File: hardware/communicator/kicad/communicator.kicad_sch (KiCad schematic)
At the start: 0 parts

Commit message: feat: add R1 detailed hardware and navigation protocol review candidate
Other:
- added sheet 00_vehicle_input (00_vehicle_input.kicad_sch)
- added sheet 00b_reverse_ov (00b_reverse_ov.kicad_sch)
- added sheet 00c_auto_5v (00c_auto_5v.kicad_sch)
- added sheet 01_usb_c (01_usb_c.kicad_sch)
- added sheet 01b_usb_limit (01b_usb_limit.kicad_sch)
- added sheet 02_system_power (02_system_power.kicad_sch)
- added sheet 03_reset (03_reset.kicad_sch)
- added sheet 03b_phy_power (03b_phy_power.kicad_sch)
- added sheet 03c_auto_qualification (03c_auto_qualification.kicad_sch)
- added sheet 12b_latch_clear (12b_latch_clear.kicad_sch)
- added sheet 14_can_connectors (14_can_connectors.kicad_sch)
- added sheet 15_gnss_ins (15_gnss_ins.kicad_sch)
- added sheet 16_barometer (16_barometer.kicad_sch)
- added sheet 17_gps_ports (17_gps_ports.kicad_sch)
- added sheet 18_gps_protection (18_gps_protection.kicad_sch)
- added sheet 19_gps_power (19_gps_power.kicad_sch)
- added sheet 20_test_points (20_test_points.kicad_sch)

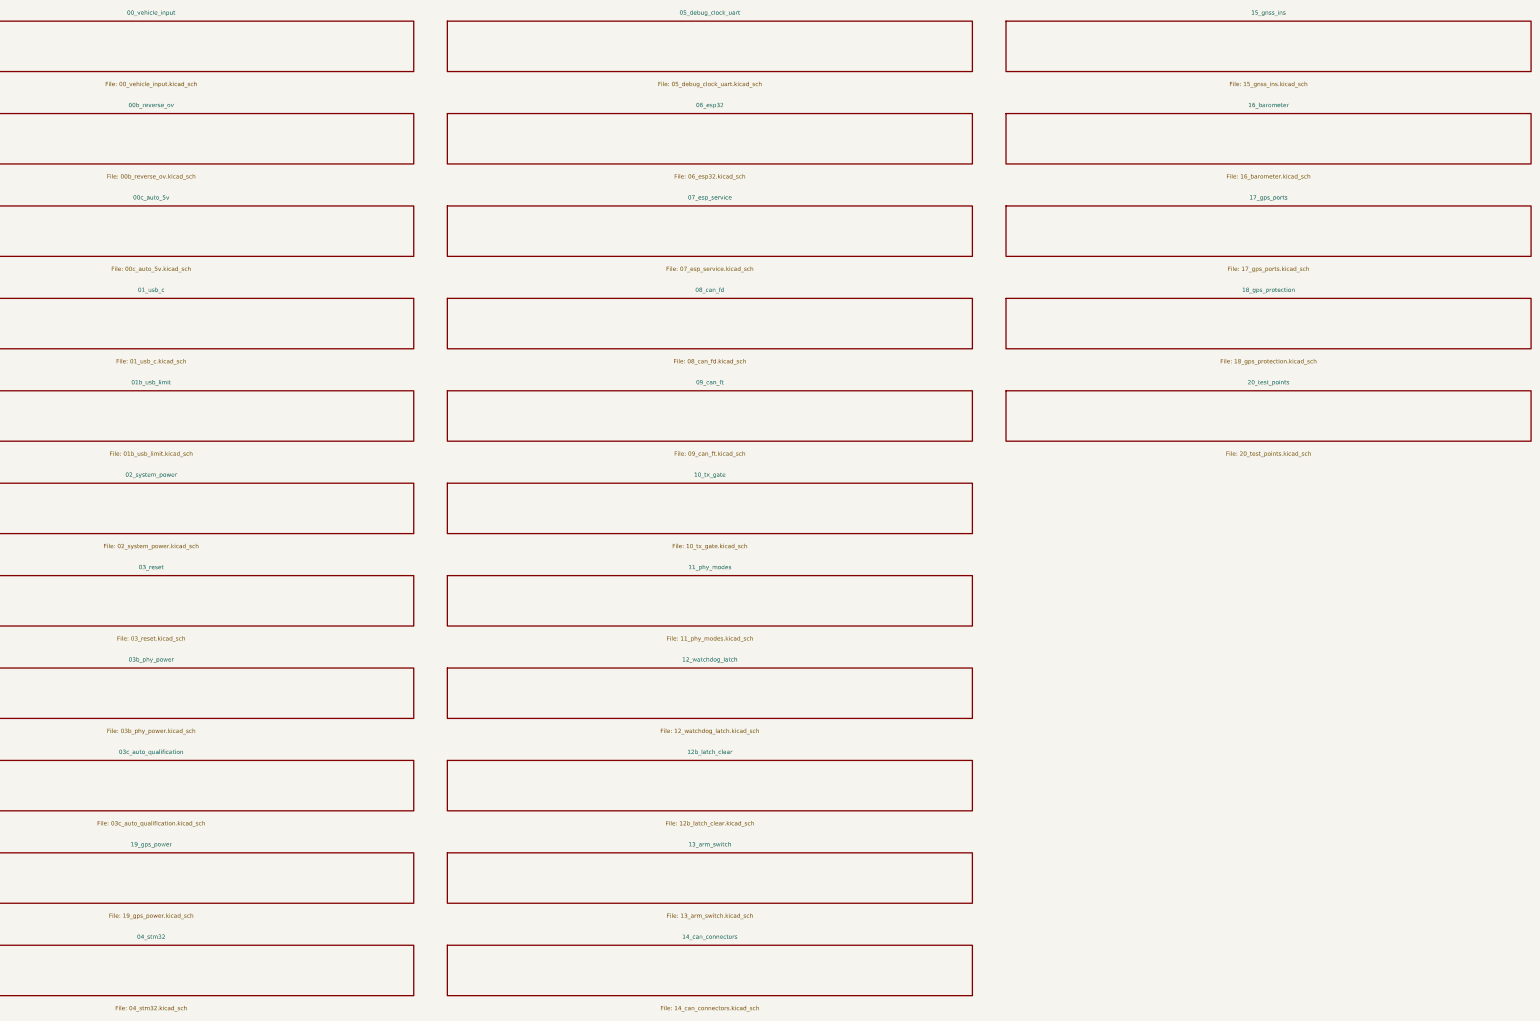
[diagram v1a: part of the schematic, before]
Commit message: fix: close hardware rail-fault paths and sensor contract gaps
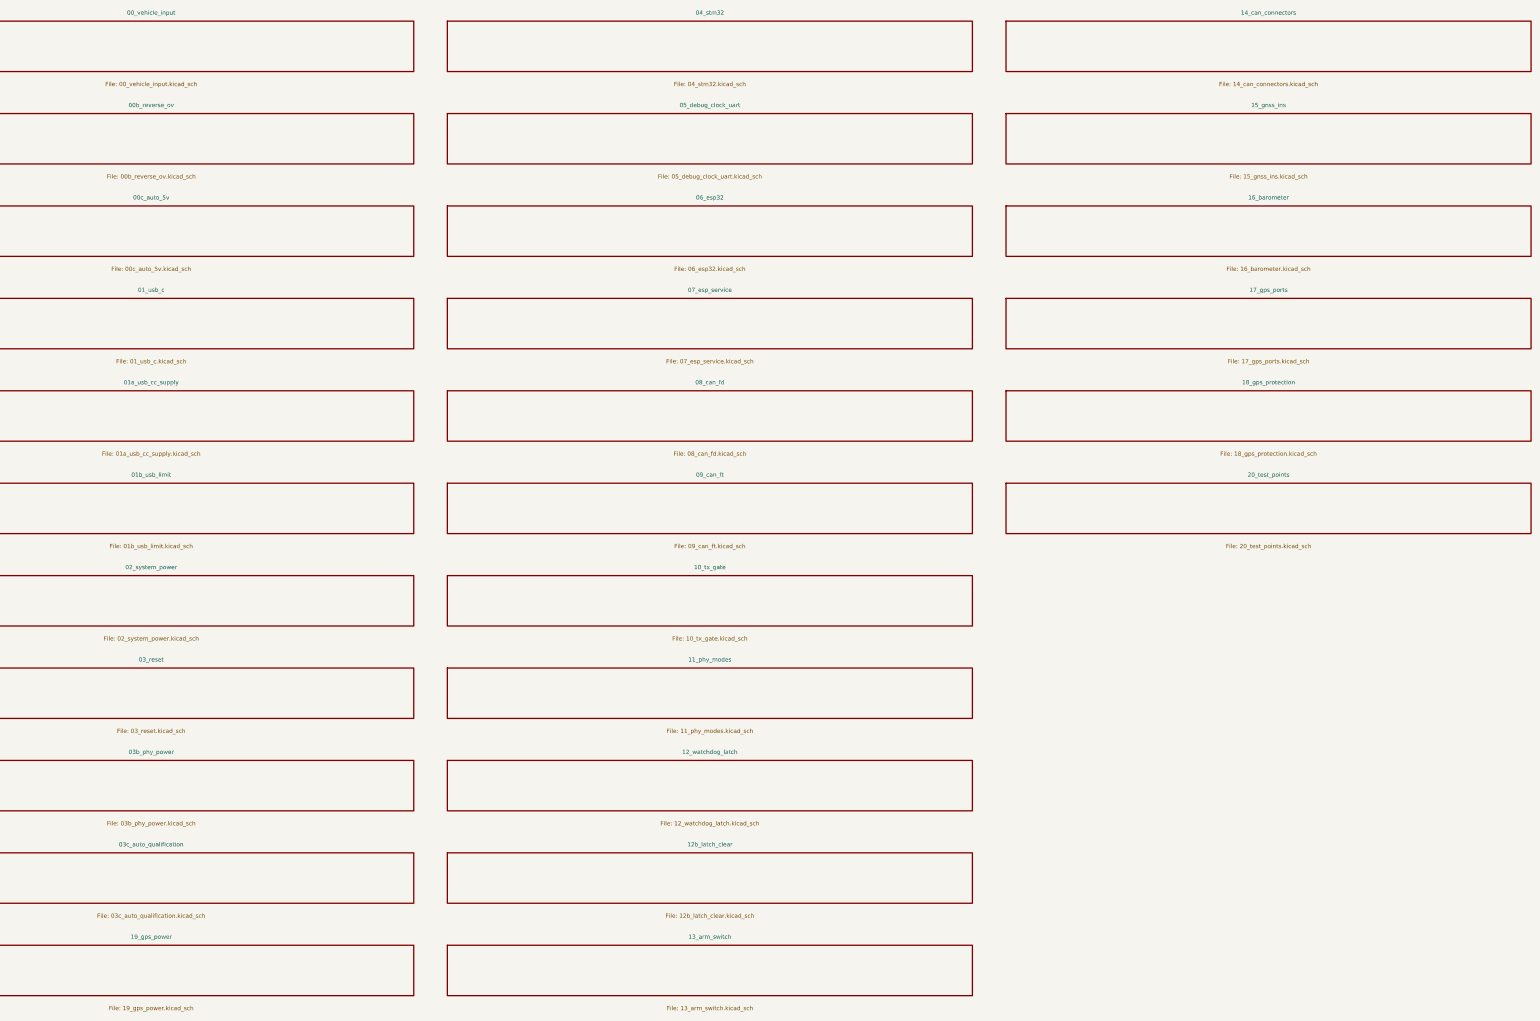
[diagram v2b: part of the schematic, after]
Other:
- added sheet 01a_usb_cc_supply (01a_usb_cc_supply.kicad_sch)

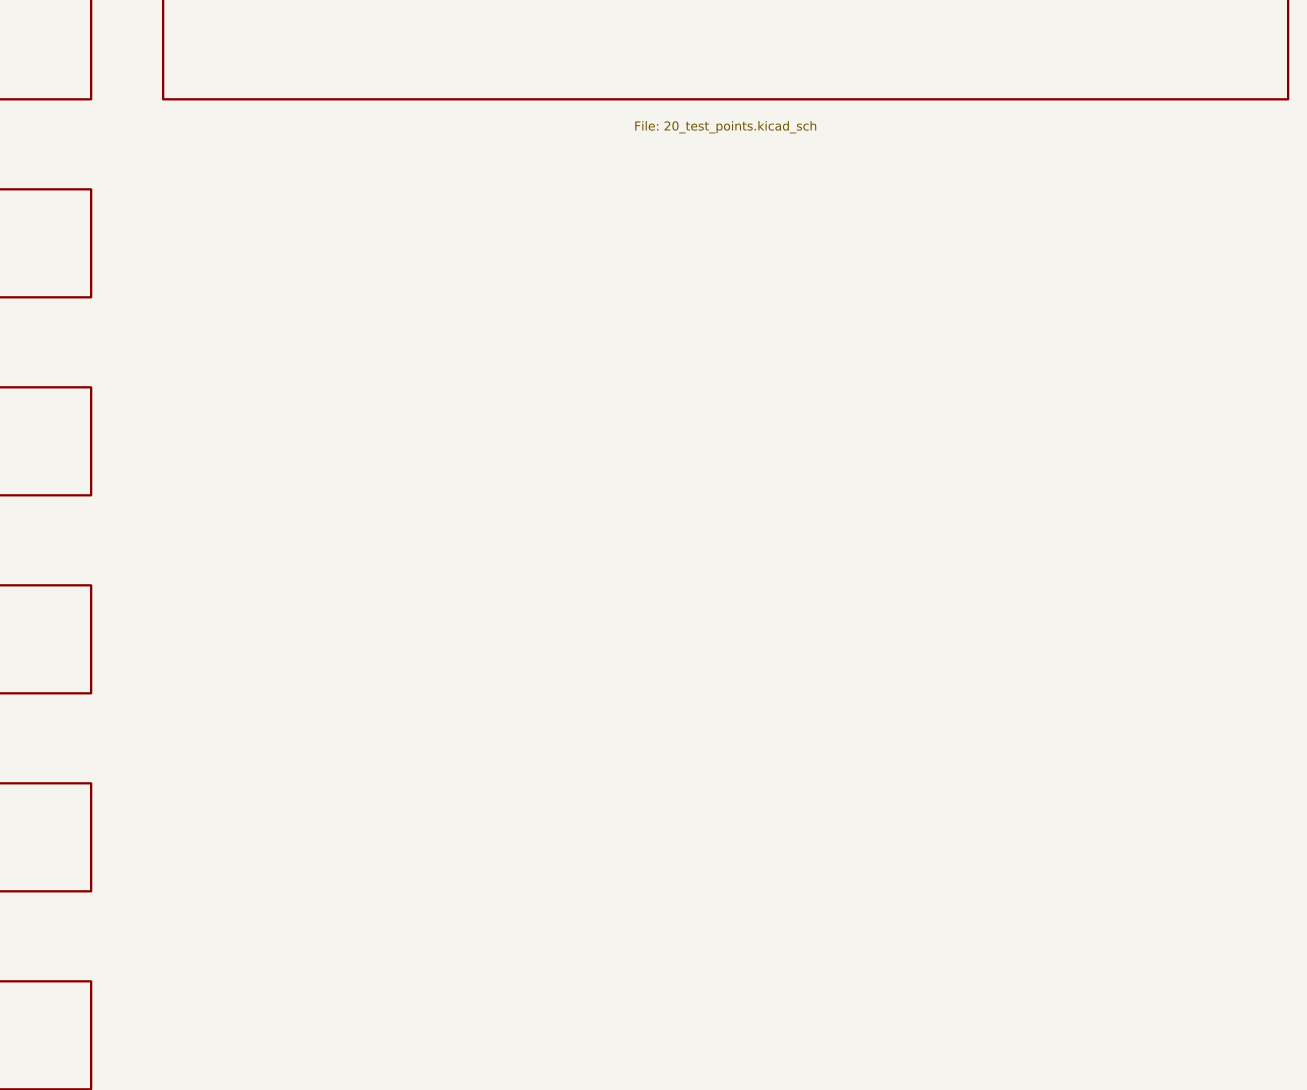
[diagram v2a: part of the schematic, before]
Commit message: Design independent OTA recovery and update N16R8 hardware
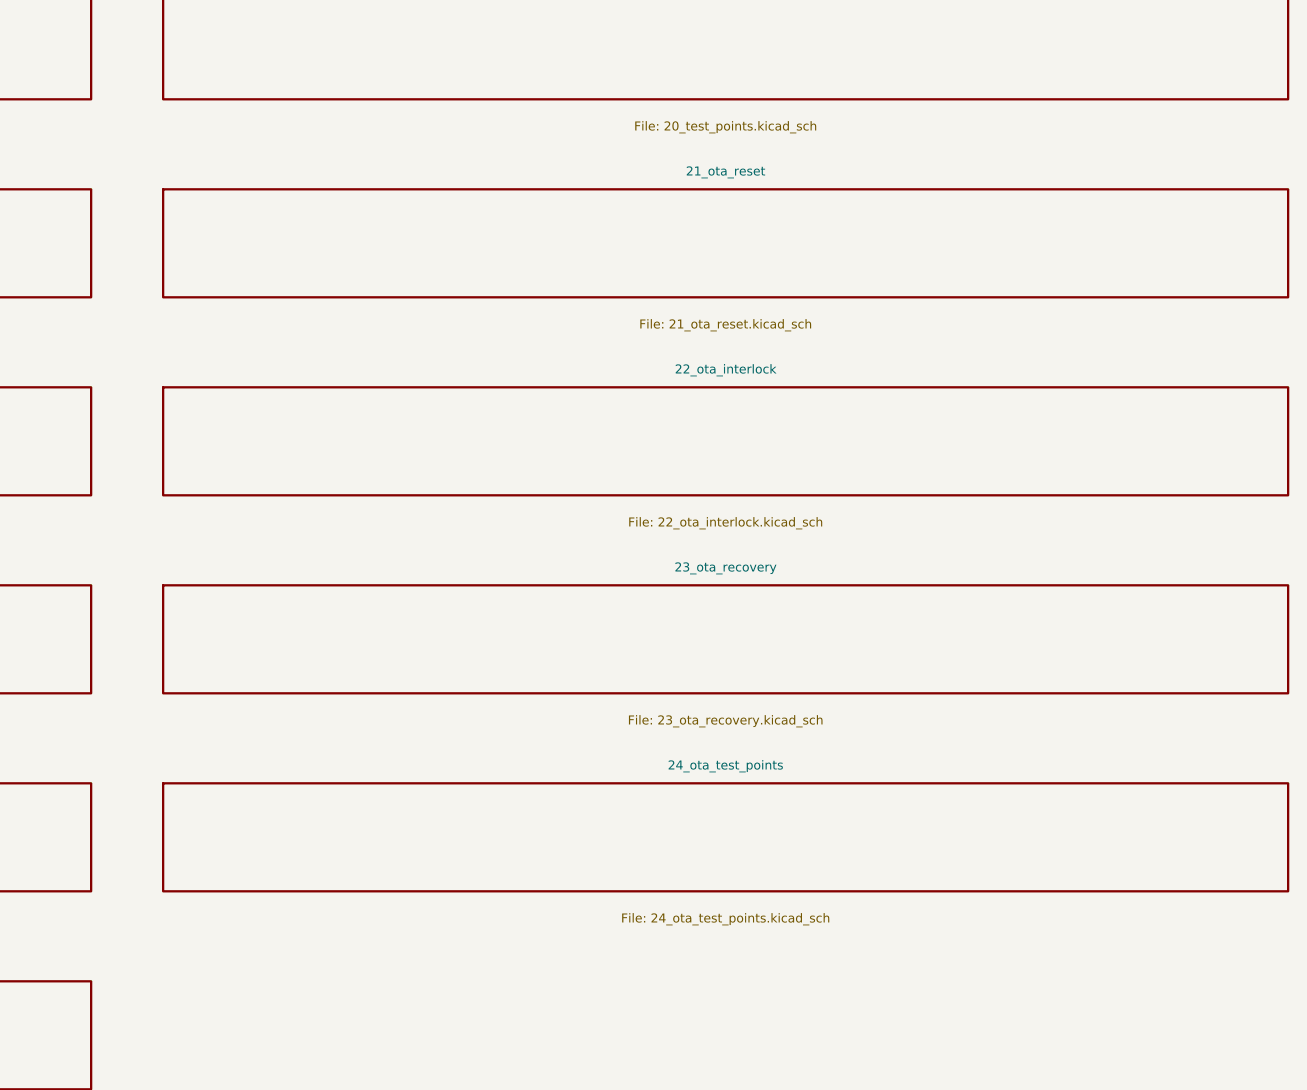
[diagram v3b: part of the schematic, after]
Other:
- added sheet 21_ota_reset (21_ota_reset.kicad_sch)
- added sheet 22_ota_interlock (22_ota_interlock.kicad_sch)
- added sheet 23_ota_recovery (23_ota_recovery.kicad_sch)
- added sheet 24_ota_test_points (24_ota_test_points.kicad_sch)
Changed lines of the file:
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@@
 (sheet (at 283 118) (size 125 12) (stroke (width 0.254) (type default)) (fill (color 0 0 0 0)) (property "Sheetname" "18_gps_protection" (at 345.5000 116.0000 0)  (effects (font (size 1.0 1.0)) )) (property "Sheetfile" "18_gps_protection.kicad_sch" (at 345.5000 133.0000 0)  (effects (font (size 1.0 1.0)) )) (instances (project "communicator" (path "/c8ff26d1-0b80-520e-ae3f-45aa29bfe092" (page "28")))))
 (sheet (at 283 140) (size 125 12) (stroke (width 0.254) (type default)) (fill (color 0 0 0 0)) (property "Sheetname" "20_test_points" (at 345.5000 138.0000 0)  (effects (font (size 1.0 1.0)) )) (property "Sheetfile" "20_test_points.kicad_sch" (at 345.5000 155.0000 0)  (effects (font (size 1.0 1.0)) )) (instances (project "communicator" (path "/c8ff26d1-0b80-520e-ae3f-45aa29bfe092" (page "29")))))
+(sheet (at 283 162) (size 125 12) (stroke (width 0.254) (type default)) (fill (color 0 0 0 0)) (property "Sheetname" "21_ota_reset" (at 345.5000 160.0000 0)  (effects (font (size 1.0 1.0)) )) (property "Sheetfile" "21_ota_reset.kicad_sch" (at 345.5000 177.0000 0)  (effects (font (size 1.0 1.0)) )) (instances (project "communicator" (path "/c8ff26d1-0b80-520e-ae3f-45aa29bfe092" (page "30")))))
+(sheet (at 283 184) (size 125 12) (stroke (width 0.254) (type default)) (fill (color 0 0 0 0)) (property "Sheetname" "22_ota_interlock" (at 345.5000 182.0000 0)  (effects (font (size 1.0 1.0)) )) (property "Sheetfile" "22_ota_interlock.kicad_sch" (at 345.5000 199.0000 0)  (effects (font (size 1.0 1.0)) )) (instances (project "communicator" (path "/c8ff26d1-0b80-520e-ae3f-45aa29bfe092" (page "31")))))
+(sheet (at 283 206) (size 125 12) (stroke (width 0.254) (type default)) (fill (color 0 0 0 0)) (property "Sheetname" "23_ota_recovery" (at 345.5000 204.0000 0)  (effects (font (size 1.0 1.0)) )) (property "Sheetfile" "23_ota_recovery.kicad_sch" (at 345.5000 221.0000 0)  (effects (font (size 1.0 1.0)) )) (instances (project "communicator" (path "/c8ff26d1-0b80-520e-ae3f-45aa29bfe092" (page "32")))))
+(sheet (at 283 228) (size 125 12) (stroke (width 0.254) (type default)) (fill (color 0 0 0 0)) (property "Sheetname" "24_ota_test_points" (at 345.5000 226.0000 0)  (effects (font (size 1.0 1.0)) )) (property "Sheetfile" "24_ota_test_points.kicad_sch" (at 345.5000 243.0000 0)  (effects (font (size 1.0 1.0)) )) (instances (project "communicator" (path "/c8ff26d1-0b80-520e-ae3f-45aa29bfe092" (page "33")))))
 (sheet_instances (path "/" (page "1")))
 )
